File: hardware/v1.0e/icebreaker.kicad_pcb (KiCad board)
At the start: 4 copper layers, 73 x 37 mm, 191 parts, among them J1 Jumper, J10 Jumper, J11 Jumper, J12 Jumper, J13 Jumper, J14 Jumper, J15 Jumper, J16 Jumper, J17 Jumper, J18 Jumper, J19 Jumper, J2 Jumper, J20 Flash, J21 PMOD, J22 PMOD, J23 PMOD, J24 PMOD, J25 RGB Led, J26 5V AUX, J27 5V AUX, J28 CRESET, J29 Jumper, J3 Jumper, J30 Jumper, J31 RGB Led, J32 WS2812, J33 RGB Led, J34 SADD, J4 Jumper, J5 Jumper, J6 Jumper, J7 Jumper, J8 Jumper, J9 Jumper, P1 pkl_USB_OTG, P2 UP, P3 UP, P4 UP, P5 UP, P6 RAM_CS, Q1 BSS138, SW1 TACT, SW2 TACT, SW3 TACT, SW4 TACT, U1 93C46B-SOT-23-6, U2 3.3V, U3 1V2, U4 FT2232H, U5 W25Q, U6 ICE5LP4K-SG48, U7 12MHz

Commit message: Corrected the RGB pin numbering.
The original symbol was based on the older ice5lp not ice40up. The
numbering/naming of those pins changed. Now it should be fixed.

Fixes #31 and #32
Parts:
- U6: value ICE5LP4K-SG48 -> ICE40UP5K-SG48
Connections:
- net /EB_OD2 renamed /EB_OD0
- net /ET_OD2 renamed /ET_OD0
- D11 pad 1: /~LED_RGB2 -> /~LED_RGB0
- D11 pad 3: /~LED_RGB0 -> /~LED_RGB2
- J25 pad 2: /~LED_RGB2 -> /~LED_RGB0
- J25 pad 4: /~LED_RGB0 -> /~LED_RGB2
- U6 pad 39: /~LED_RGB2 -> /~LED_RGB0
- U6 pad 41: /~LED_RGB0 -> /~LED_RGB2
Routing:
- net /~LED_RGB2: track 42.8 -> 39.5 mm, vias 2 -> 3
- net /~LED_RGB0: track 39.5 -> 42.8 mm, vias 3 -> 2
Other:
- board text added: "D 0"
- board text added: "D0"
- board text removed: "D 2"
- board text removed: "D2"

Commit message: Corrected one of the ear net names to match the RGB led net changes.
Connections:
- net /ET_O2 renamed /ET_O0
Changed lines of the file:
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@@
   (net 122 /~LED_RGB0)
   (net 123 /VPP_2V5)
-  (net 124 /ET_O2)
-  (net 125 /ET_OD0)
-  (net 126 /EB_OD0)
+  (net 124 /ET_OD0)
+  (net 125 /EB_OD0)
+  (net 126 /ET_O0)
   (net_class Default "This is the default net class."
     (clearance 0.15)
@@
     (add_net /ET_5V)
     (add_net /ET_GND)
-    (add_net /ET_O2)
+    (add_net /ET_O0)
     (add_net /ET_OD0)
     (add_net /ET_OD1)
@@
       (net 117 /EB_3V3))
     (pad 1 smd roundrect (at -0.75 0 90) (size 0.6 0.9) (layers F.Cu F.Mask) (roundrect_rratio 0.25)
-      (net 126 /EB_OD0))
+      (net 125 /EB_OD0))
     (model ${KISYS3DMOD}/Resistor_SMD.3dshapes/R_0603_1608Metric.stepX
       (at (xyz 0 0 0))
@@
       (xy 0.25 0.425)) (layer F.SilkS) (width 0.05))
     (pad 2 smd roundrect (at 0.75 0 90) (size 0.6 0.9) (layers F.Cu F.Mask) (roundrect_rratio 0.25)
-      (net 124 /ET_O2))
+      (net 126 /ET_O0))
     (pad 1 smd roundrect (at -0.75 0 90) (size 0.6 0.9) (layers F.Cu F.Mask) (roundrect_rratio 0.25)
       (net 115 /ET_5V))
@@
       (xy 0.25 0.425)) (layer F.SilkS) (width 0.05))
     (pad 2 smd roundrect (at 0.75 0 180) (size 0.6 0.9) (layers F.Cu F.Mask) (roundrect_rratio 0.25)
-      (net 125 /ET_OD0))
+      (net 124 /ET_OD0))
     (pad 1 smd roundrect (at -0.75 0 180) (size 0.6 0.9) (layers F.Cu F.Mask) (roundrect_rratio 0.25)
       (net 114 /ET_3V3))
@@
       (net 115 /ET_5V))
     (pad 2 thru_hole oval (at 0 2.54 270) (size 1.7 1.7) (drill 1) (layers *.Cu *.Mask)
-      (net 124 /ET_O2))
+      (net 126 /ET_O0))
     (pad 1 thru_hole rect (at 0 0 270) (size 1.7 1.7) (drill 1) (layers *.Cu *.Mask)
       (net 116 /ET_GND))
@@
       (net 118 /EB_OD1))
     (pad 2 thru_hole oval (at -2.54 0 270) (size 1.7 1.7) (drill 1) (layers *.Cu *.Mask)
-      (net 126 /EB_OD0))
+      (net 125 /EB_OD0))
     (pad 3 thru_hole oval (at 0 -2.54 270) (size 1.7 1.7) (drill 1) (layers *.Cu *.Mask))
     (pad 4 thru_hole oval (at -2.54 -2.54 270) (size 1.7 1.7) (drill 1) (layers *.Cu *.Mask))
@@
       (net 117 /EB_3V3))
     (pad 2 thru_hole oval (at -2.54 0 90) (size 1.7 1.7) (drill 1) (layers *.Cu *.Mask)
-      (net 126 /EB_OD0))
+      (net 125 /EB_OD0))
     (pad 3 thru_hole oval (at 0 2.54 90) (size 1.7 1.7) (drill 1) (layers *.Cu *.Mask)
       (net 119 /EB_GND))
@@
     (pad 1 thru_hole rect (at 0 0 270) (size 1.7 1.7) (drill 1) (layers *.Cu *.Mask))
     (pad 2 thru_hole oval (at -2.54 0 270) (size 1.7 1.7) (drill 1) (layers *.Cu *.Mask)
-      (net 125 /ET_OD0))
+      (net 124 /ET_OD0))
     (pad 3 thru_hole oval (at 0 -2.54 270) (size 1.7 1.7) (drill 1) (layers *.Cu *.Mask))
     (pad 4 thru_hole oval (at -2.54 -2.54 270) (size 1.7 1.7) (drill 1) (layers *.Cu *.Mask))
@@
     (fp_line (start 0.76 1.58) (end -0.7 1.58) (layer F.SilkS) (width 0.12))
     (pad 1 smd roundrect (at -1 -0.95 180) (size 0.9 0.8) (layers F.Cu F.Mask) (roundrect_rratio 0.25)
-      (net 125 /ET_OD0))
+      (net 124 /ET_OD0))
     (pad 2 smd roundrect (at -1 0.95 180) (size 0.9 0.8) (layers F.Cu F.Mask) (roundrect_rratio 0.25)
       (net 116 /ET_GND))
     (pad 3 smd roundrect (at 1 0 180) (size 0.9 0.8) (layers F.Cu F.Mask) (roundrect_rratio 0.25)
-      (net 124 /ET_O2))
+      (net 126 /ET_O0))
     (model ${KISYS3DMOD}/Package_TO_SOT_SMD.3dshapes/SOT-23.stepX
       (at (xyz 0 0 0))
@@
   (segment (start 84.3 33.52) (end 84.31 33.53) (width 0.15) (layer F.Cu) (net 115))
   (segment (start 84.3 31.25) (end 84.3 33.52) (width 0.15) (layer F.Cu) (net 115))
-  (segment (start 92.52 62.15) (end 93.2 61.47) (width 0.15) (layer F.Cu) (net 126))
-  (segment (start 90 62.15) (end 92.52 62.15) (width 0.15) (layer F.Cu) (net 126))
-  (segment (start 90 62.15) (end 89.45 62.7) (width 0.15) (layer F.Cu) (net 126))
-  (segment (start 85.62 62.7) (end 84.31 64.01) (width 0.15) (layer F.Cu) (net 126))
-  (segment (start 89.45 62.7) (end 85.62 62.7) (width 0.15) (layer F.Cu) (net 126))
+  (segment (start 92.52 62.15) (end 93.2 61.47) (width 0.15) (layer F.Cu) (net 125))
+  (segment (start 90 62.15) (end 92.52 62.15) (width 0.15) (layer F.Cu) (net 125))
+  (segment (start 90 62.15) (end 89.45 62.7) (width 0.15) (layer F.Cu) (net 125))
+  (segment (start 85.62 62.7) (end 84.31 64.01) (width 0.15) (layer F.Cu) (net 125))
+  (segment (start 89.45 62.7) (end 85.62 62.7) (width 0.15) (layer F.Cu) (net 125))
   (via (at 91.1 64.9) (size 0.5) (drill 0.3) (layers F.Cu B.Cu) (net 117))
   (segment (start 90 64.85) (end 91.05 64.85) (width 0.15) (layer F.Cu) (net 117))
@@
   (segment (start 70.246447 48.746447) (end 70.192893 48.746447) (width 0.15) (layer F.Cu) (net 123))
   (segment (start 70.192893 48.746447) (end 69.36967 49.56967) (width 0.15) (layer F.Cu) (net 123))
-  (segment (start 92.79 31.4) (end 93.2 30.99) (width 0.15) (layer F.Cu) (net 125))
-  (segment (start 90.05 31.4) (end 92.79 31.4) (width 0.15) (layer F.Cu) (net 125))
-  (segment (start 89.25 30.6) (end 90.05 31.4) (width 0.15) (layer F.Cu) (net 125))
-  (segment (start 88.3 31.55) (end 89.25 30.6) (width 0.15) (layer F.Cu) (net 125))
-  (segment (start 87.9 31.55) (end 88.3 31.55) (width 0.15) (layer F.Cu) (net 125))
-  (segment (start 85.05 29.75) (end 85.9 30.6) (width 0.15) (layer F.Cu) (net 124))
-  (segment (start 84.3 29.75) (end 85.05 29.75) (width 0.15) (layer F.Cu) (net 124))
-  (segment (start 85.9 32.58) (end 86.85 33.53) (width 0.15) (layer F.Cu) (net 124))
-  (segment (start 85.9 30.6) (end 85.9 32.58) (width 0.15) (layer F.Cu) (net 124))
+  (segment (start 92.79 31.4) (end 93.2 30.99) (width 0.15) (layer F.Cu) (net 124))
+  (segment (start 90.05 31.4) (end 92.79 31.4) (width 0.15) (layer F.Cu) (net 124))
+  (segment (start 89.25 30.6) (end 90.05 31.4) (width 0.15) (layer F.Cu) (net 124))
+  (segment (start 88.3 31.55) (end 89.25 30.6) (width 0.15) (layer F.Cu) (net 124))
+  (segment (start 87.9 31.55) (end 88.3 31.55) (width 0.15) (layer F.Cu) (net 124))
+  (segment (start 85.05 29.75) (end 85.9 30.6) (width 0.15) (layer F.Cu) (net 126))
+  (segment (start 84.3 29.75) (end 85.05 29.75) (width 0.15) (layer F.Cu) (net 126))
+  (segment (start 85.9 32.58) (end 86.85 33.53) (width 0.15) (layer F.Cu) (net 126))
+  (segment (start 85.9 30.6) (end 85.9 32.58) (width 0.15) (layer F.Cu) (net 126))
   (zone (net 26) (net_name GND) (layer F.Cu) (hatch edge 0.508)
     (connect_pads (clearance 0.15))

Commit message: Corrected silkscreen for the RGB connector.
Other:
- board text added: "RGB0 RGB1"
- board text added: "RGB2 1V2"
- board text removed: "RGB0 1V2"
- board text removed: "RGB2 RGB1"
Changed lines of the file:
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@@
     (effects (font (size 0.75 0.75) (thickness 0.1875)))
   )
-  (gr_text 0 (at 46.21 60.835) (layer F.SilkS)
+  (gr_text 2 (at 46.21 60.835) (layer F.SilkS)
     (effects (font (size 0.75 0.75) (thickness 0.1875)))
   )
@@
     (effects (font (size 0.75 0.75) (thickness 0.1875)))
   )
-  (gr_text 2 (at 43.67 60.835) (layer F.SilkS)
+  (gr_text 0 (at 43.67 60.835) (layer F.SilkS)
     (effects (font (size 0.75 0.75) (thickness 0.1875)))
   )
@@
     (effects (font (size 1 0.75) (thickness 0.1875)) (justify mirror))
   )
-  (gr_text "RGB2\nRGB1" (at 42.4 58.8) (layer B.SilkS)
+  (gr_text "RGB0\nRGB1" (at 42.4 58.8) (layer B.SilkS)
     (effects (font (size 1 0.6) (thickness 0.15)) (justify mirror))
   )
-  (gr_text "RGB0\n1V2" (at 44.95 58.8) (layer B.SilkS)
+  (gr_text "RGB2\n1V2" (at 44.95 58.8) (layer B.SilkS)
     (effects (font (size 1 0.6) (thickness 0.15)) (justify mirror))
   )

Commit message: Added exact FPGA EEPROM type and datasheet link.
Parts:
- U5: value W25Q -> W25Q128JV-DTR
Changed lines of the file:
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@@
       (effects (font (size 1 1) (thickness 0.15)))
     )
-    (fp_text value W25Q (at 0 1.5) (layer F.Fab)
+    (fp_text value W25Q128JV-DTR (at 0 1.5) (layer F.Fab)
       (effects (font (size 1 1) (thickness 0.15)))
     )

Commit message: Replaced/added the null logo to the boards.
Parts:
- added REF**: null_Logo_SilkS_5mm, pkl_logos:null_Logo_SilkS_5mm, B.Cu at (42.2, 47.2)
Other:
- board text added: "NULL"

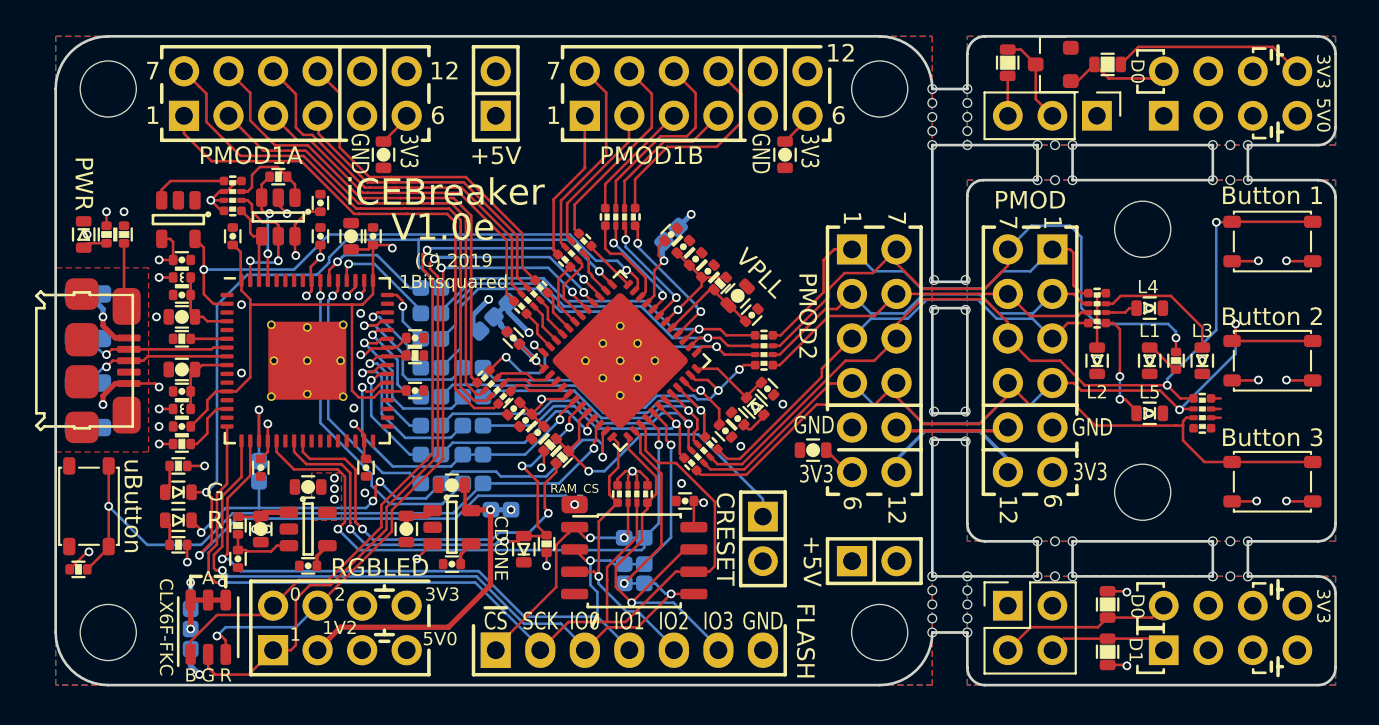
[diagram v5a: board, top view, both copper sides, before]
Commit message: Updated all design files to KiCad V8.0.6.
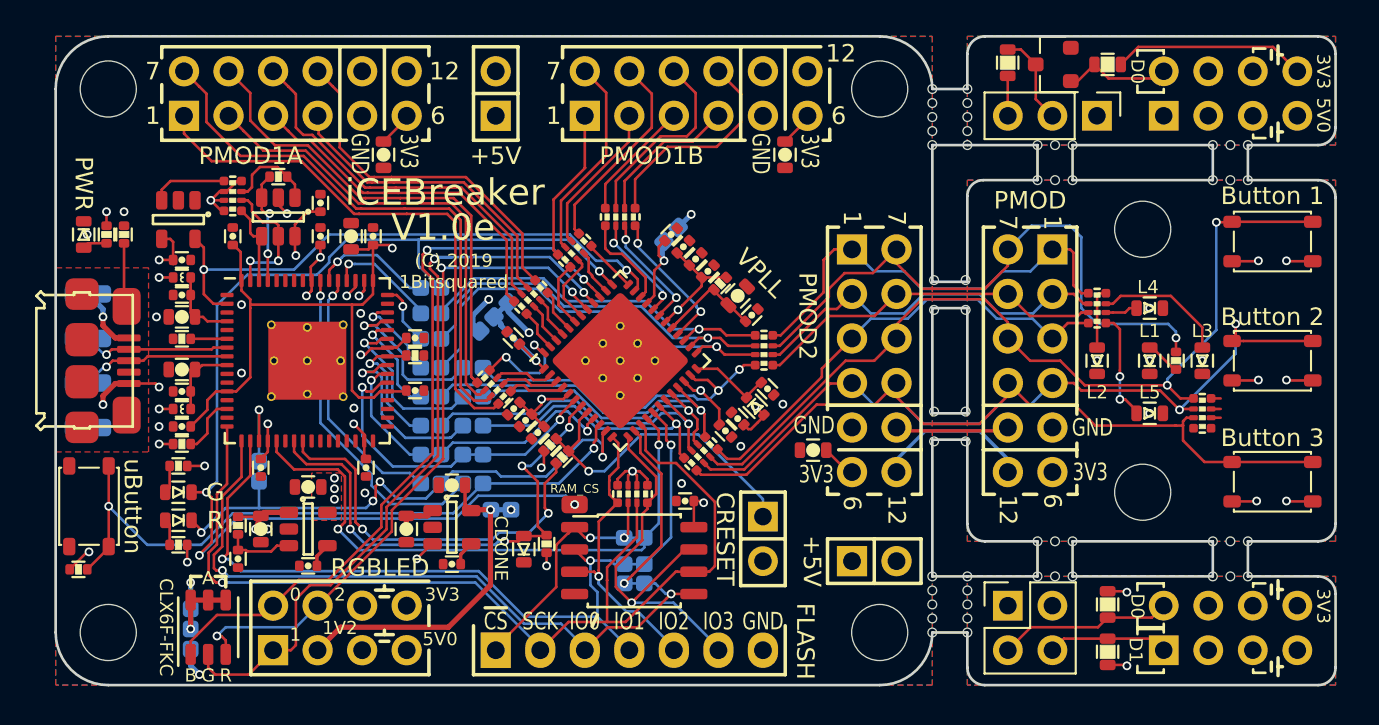
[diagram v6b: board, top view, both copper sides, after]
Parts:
- D2: value ~~800mVf -> ~800mVf
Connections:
- net /FLASH_~HLD~|~RST~|IO3 renamed /FLASH_~{HLD}|~{RST}|IO3
- net /FLASH_~WP~|IO2 renamed /FLASH_~{WP}|IO2
- net /xFIFO_~RD renamed /xFIFO_~{RD}
- net /xFIFO_~RXF renamed /xFIFO_~{RXF}
- net /xFIFO_~TXE renamed /xFIFO_~{TXE}
- net /xFIFO_~WR renamed /xFIFO_~{WR}
- net /~BUTTON renamed /~{BUTTON}
- net /~LEDG renamed /~{LEDG}
- net /~LEDR renamed /~{LEDR}
- net /~LED_RGB0 renamed /~{LED_RGB0}
- net /~LED_RGB1 renamed /~{LED_RGB1}
- net /~LED_RGB2 renamed /~{LED_RGB2}
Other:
- net class Default removed
- board text added: "~{CS}"
- board text removed: "~CS"
